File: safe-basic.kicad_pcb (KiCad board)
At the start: 10 x 10 mm, 1 part

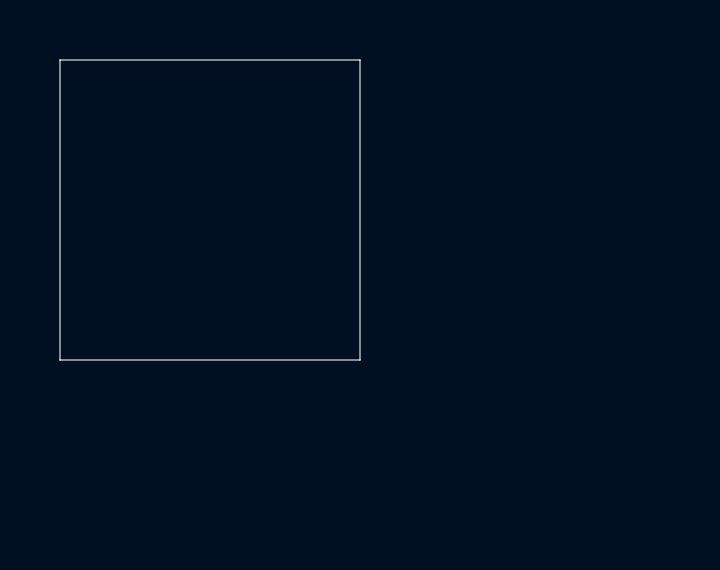
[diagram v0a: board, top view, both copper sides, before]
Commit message: test: real KiCad board geometry revision for #1161 visual diff acceptance
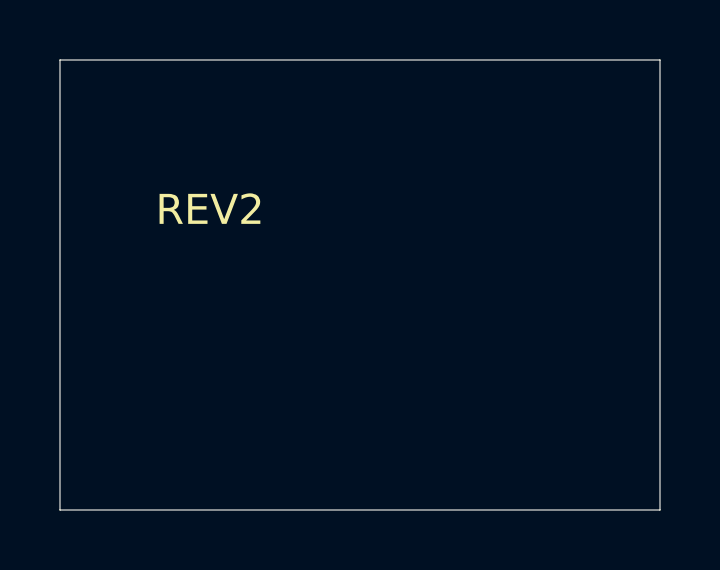
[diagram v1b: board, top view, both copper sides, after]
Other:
- board size 10 x 10 mm -> 20 x 15 mm
- board text added: "REV2"
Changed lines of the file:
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@@
   (version 20250114)
   (title_block (title "safe-basic") (rev "v1.0"))
-  (gr_rect (start 0 0) (end 10 10) (layer "Edge.Cuts"))
+  (gr_rect (start 0 0) (end 20 15) (layer "Edge.Cuts"))
+  (gr_text "REV2" (at 5 5) (layer "F.SilkS") (effects (font (size 1 1) (thickness 0.15))))
   (footprint "Resistor_SMD:R_0603"
     (property "Reference" "R1")

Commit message: test: preserve PCB outline for real base/head visual diff acceptance
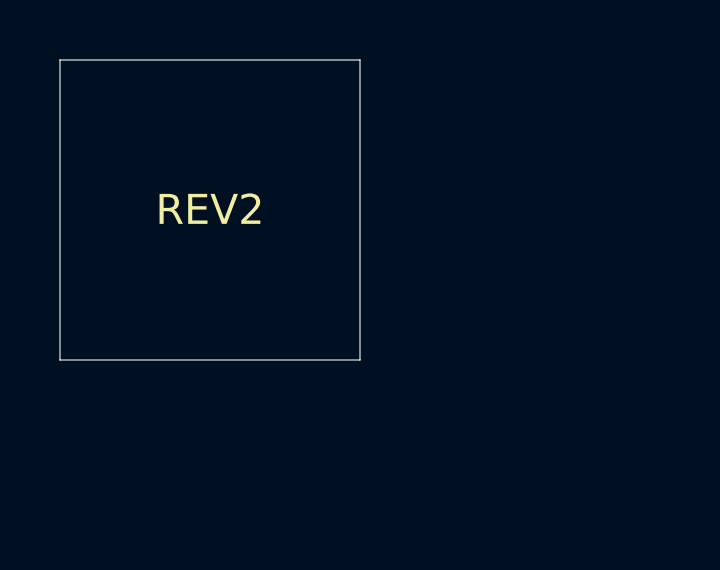
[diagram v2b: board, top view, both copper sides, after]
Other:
- board size 20 x 15 mm -> 10 x 10 mm
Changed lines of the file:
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@@
   (version 20250114)
   (title_block (title "safe-basic") (rev "v1.0"))
-  (gr_rect (start 0 0) (end 20 15) (layer "Edge.Cuts"))
+  (gr_rect (start 0 0) (end 10 10) (layer "Edge.Cuts"))
   (gr_text "REV2" (at 5 5) (layer "F.SilkS") (effects (font (size 1 1) (thickness 0.15))))
   (footprint "Resistor_SMD:R_0603"
